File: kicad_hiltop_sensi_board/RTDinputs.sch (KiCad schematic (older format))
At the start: 28 parts, among them SW2 SW_DIP_x04, SW3 SW_DIP_x04, SW4 SW_DIP_x04, SW5 SW_DIP_x04, U10 MAX31865, U11 MAX31865, U8 MAX31865, U9 MAX31865

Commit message: Sensi Board Complete
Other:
- note added: "1\nOFF\nON\nOFF"
- note added: "2 Wire\n3 Wire\n4 Wire"
- note added: "2\nON\nOFF\nON"
- note added: "3\nON\nOFF\nOFF"
- note added: "4\nON\nON\nOFF"
- note added: "RTD SW Sett Per RTD"
- note removed: "J1\nLeft Position\nRight Position\nLeft Position"
- note removed: "J2\nClose\nClose\nOpen"
- note removed: "J3\nClose\nOpen\nOpen"
- note removed: "RTD Config\n2 Wire\n3 Wire\n4 Wire"
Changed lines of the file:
@@
 	7700 9375 7825 9375
 Connection ~ 7700 9375
-Text Notes 4430 10570 0    60   ~ 0
-RTD Config\n2 Wire\n3 Wire\n4 Wire
-Text Notes 5020 10570 0    60   ~ 0
-J1\nLeft Position\nRight Position\nLeft Position
-Text Notes 5755 10560 0    60   ~ 0
-J2\nClose\nClose\nOpen
-Text Notes 6090 10555 0    60   ~ 0
-J3\nClose\nOpen\nOpen
+Text Notes 4750 10545 0    60   ~ 0
+2 Wire\n3 Wire\n4 Wire
+Text Notes 5095 10545 0    60   ~ 0
+1\nOFF\nON\nOFF
+Text Notes 4815 10645 0    60   ~ 0
+Default Config 3 Wire\n
+Text Notes 5300 10545 0    60   ~ 0
+2\nON\nOFF\nON
+Text Notes 5510 10545 0    60   ~ 0
+3\nON\nOFF\nOFF
+Text Notes 5715 10545 0    60   ~ 0
+4\nON\nON\nOFF
 Wire Notes Line
-	4420 10590 6360 10590
+	5900 10555 4735 10555
 Wire Notes Line
-	6360 10180 4420 10180
+	4735 10555 4735 10160
 Wire Notes Line
-	4420 10290 6360 10290
+	4735 10160 5900 10160
 Wire Notes Line
-	6050 10590 6050 10180
+	5065 10555 5065 10160
 Wire Notes Line
-	5690 10590 5690 10180
+	5280 10555 5280 10160
 Wire Notes Line
-	4970 10590 4970 10180
-Text Notes 4860 10690 0    60   ~ 0
-Default Config 3 Wire\n
+	5485 10555 5485 10160
 Wire Notes Line
-	4420 10700 6360 10700
+	5700 10555 5700 10160
 Wire Notes Line
-	6360 10180 6360 10700
+	5900 10255 4735 10255
 Wire Notes Line
-	4420 10180 4420 10700
+	4735 10560 4735 10665
+Wire Notes Line
+	4735 10665 5900 10665
+Wire Notes Line
+	5900 10160 5900 10665
+Text Notes 4835 10155 0    60   ~ 0
+RTD SW Sett Per RTD
 $EndSCHEMATC

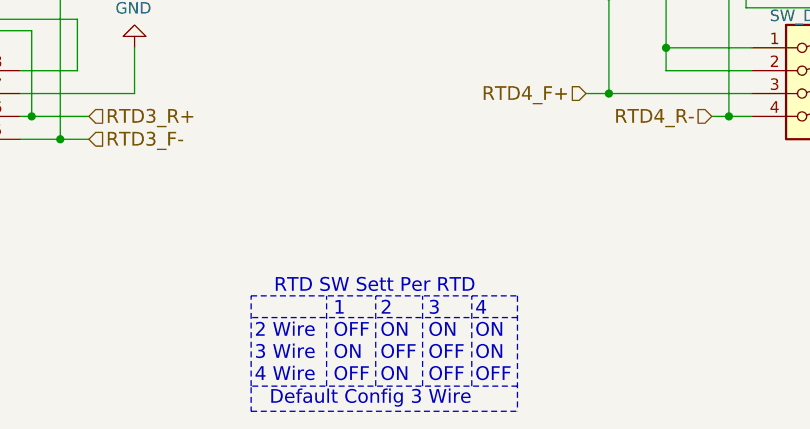
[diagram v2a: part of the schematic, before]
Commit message: Sensi Board updated RTD table
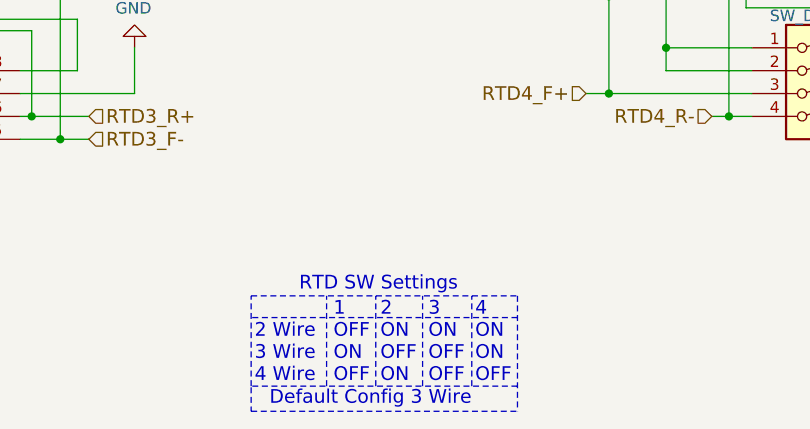
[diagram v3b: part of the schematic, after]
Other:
- note added: "RTD SW Settings"
- note removed: "RTD SW Sett Per RTD"
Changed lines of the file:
@@
 Wire Notes Line
 	5900 10160 5900 10665
-Text Notes 4835 10155 0    60   ~ 0
-RTD SW Sett Per RTD
+Text Notes 4945 10145 0    60   ~ 0
+RTD SW Settings
 $EndSCHEMATC
